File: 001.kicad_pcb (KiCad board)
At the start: 2 copper layers, 74.7 x 96.8 mm, 57 parts, among them J1 CONN_01X02, J10 TEST_1P, J11 TEST_1P, J12 TEST_1P, J13 TEST_1P, J14 TEST_1P, J15 TEST_1P, J16 TEST_1P, J2 TEST_1P, J3 TEST_1P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

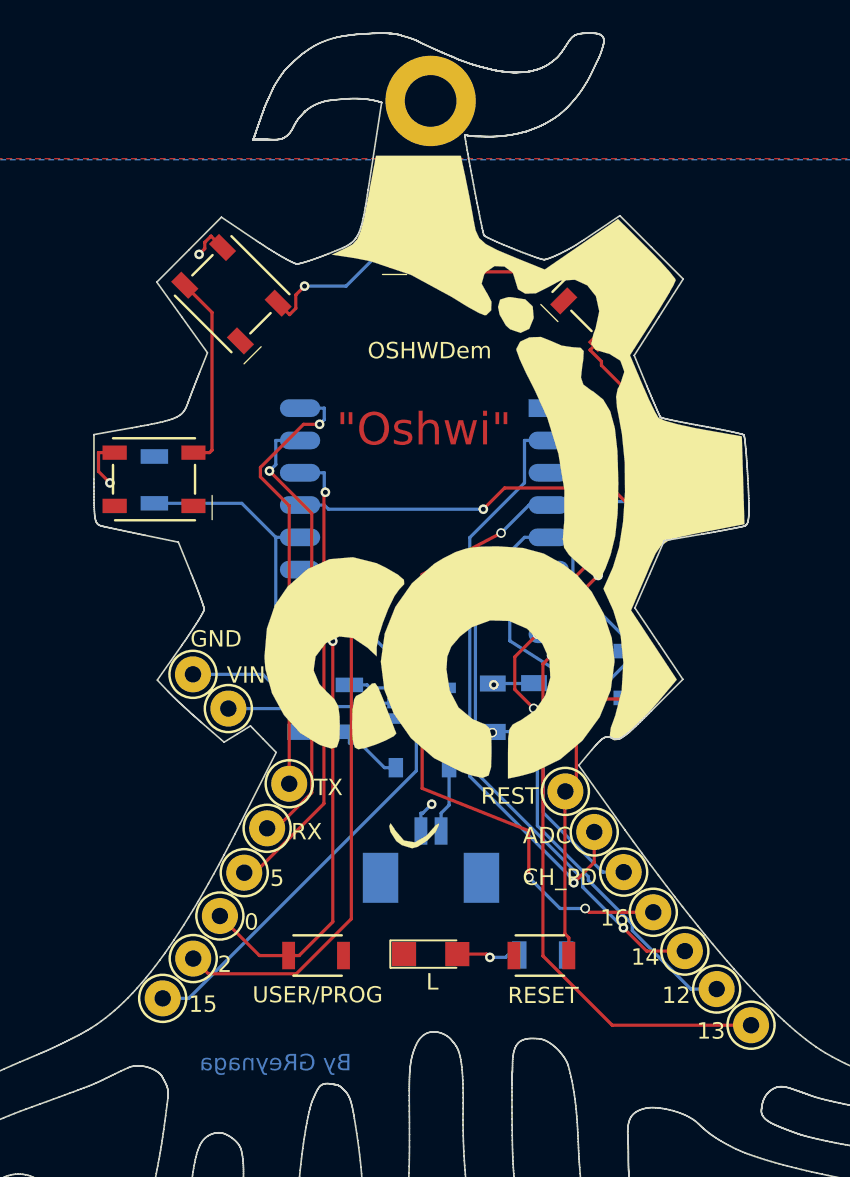
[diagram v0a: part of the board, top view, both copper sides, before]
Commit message: Final Release of OSHWDem Badge 2017
Final Release of OSHWDem Badge with PCBWay sponsorship
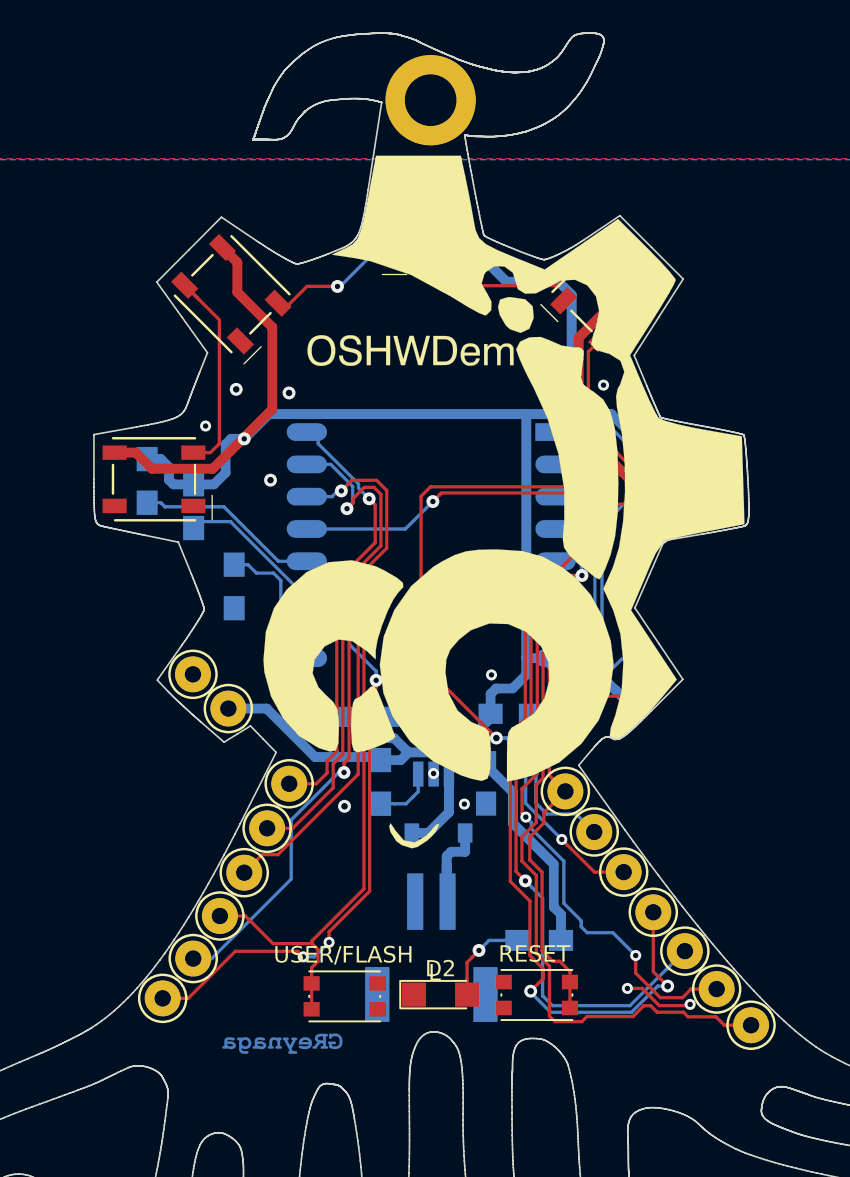
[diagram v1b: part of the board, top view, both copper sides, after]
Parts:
- removed G1***: LOGO, Mazmaker:mazmaker_700
- added BricoLabs-14***: LOGO, varios:bricolabs-14, B.Cu at (130.1, 52.3)
- added G***: LOGO, varios:OSHWDem-4, F.Cu at (129.4, 61.7)
- added GBSilk***: LOGO, varios:greynaga6-2, B.Cu at (121.3, 104.6)
- added GS***: v, varios:greynaga6-2-cooper, B.Cu at (121.3, 104.6)
- added PCBway-3: LOGO, varios:pcbway3, B.Cu at (145.1, 106.9)
- added R6: 10k, Resistors_SMD:R_0805_HandSoldering, B.Cu at (118.4, 76.4)
- added R7: 10k, Resistors_SMD:R_0805_HandSoldering, B.Cu at (115.8, 71.4)
- C1, C2, C3, C4: footprint Capacitors_SMD:C_1206 -> Capacitors_SMD:C_0805_HandSoldering
- J1: footprint Connectors_Molex:Molex_PicoBlade_53261-0271_02x1.25mm_Angled -> Connectors_JST:JST_PH_S2B-PH-SM4-TB_02x2.00mm_Angled
- R1, R2, R3, R4, R5: footprint Resistors_SMD:R_1206 -> Resistors_SMD:R_0805_HandSoldering
- SW1, SW2: footprint Wickerlib:SWITCH-OMRON-MOMENTARY-SMD-B3U-1000P -> kmr2:SW_SPST_KMR2
- moved J1 5.80 mm to (130.6, 98.8)
- moved R5 4.95 mm to (127.4, 88.5), turned to 270 degrees
- moved C2 4.71 mm to (133.9, 88.6), turned to 270 degrees
- moved C1 4.20 mm to (126.6, 84.5), turned to 180 degrees
- moved D1 4.17 mm to (131.0, 91.7)
- moved U2 3.13 mm to (130.7, 86.7), turned to 90 degrees
- moved R1 3.04 mm to (143.7, 71.4)
- moved SW2 2.83 mm to (137.1, 101.7)
- moved D2 2.58 mm to (131.1, 101.7)
- moved SW1 2.53 mm to (125.2, 101.8)
- moved U1 1.54 mm to (137.6, 66.8)
- moved C4 1.49 mm to (135.5, 84.3), turned to 0 degrees
- moved R2 0.93 mm to (137.2, 98.3)
- moved C3 0.56 mm to (146.8, 69.7)
- moved R4 0.51 mm to (143.2, 81.9)
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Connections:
- SW1 pad 2: GPIO0 -> GND
- SW2 pad 2: REST -> GND
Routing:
- net +3.3V: track 48.7 -> 161.1 mm, vias 13 -> 3
- net GND: track 24.0 -> 9.82 mm, vias 5 -> 20
- net REST: track 38.6 -> 48.1 mm
- net VCC: track 16.4 -> 25.3 mm
- net GPIO16: track 40.3 -> 48.6 mm
- net GPIO14: track 34.4 -> 42.6 mm, vias 1 -> 2
- net GPIO15: track 35.7 -> 43.6 mm, vias 0 -> 3
- net GPIO5: track 28.1 -> 34.9 mm
- net ADC: track 35.9 -> 42.4 mm, vias 1 -> 2
- net CH_PD: track 33.3 -> 37.9 mm, vias 0 -> 5
- net Net-(LED1-Pad4): track 12.1 -> 16.7 mm
- net GPIO13: track 39.8 -> 44.0 mm
- net GPIO12: track 35.4 -> 39.1 mm, vias 0 -> 3
- net GPIO0: track 45.7 -> 49.4 mm
- net RXD: track 28.9 -> 32.2 mm
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- added copper zone on B.Cu, net GND
- removed copper zone on B.Cu, net +3.3V
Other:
- net class Default: clearance 0.15 -> 0.1524; trace_width 0.2 -> 0.1524; via_dia 0.6 -> 0.6858; via_drill 0.4 -> 0.3302
- rule trace_clearance: 0.15 -> 0.1524
- rule trace_min: 0.1 -> 0.1524
- rule via_min_drill: 0.3 -> 0.3302
- rule via_min_size: 0.4 -> 0.6858
- board text added: "Designed by"
- board text added: "RESET"
- board text added: "USER/FLASH"
- board text removed: ""Oshwi""
- board text removed: "By GReynaga"
- board text removed: "Designed"
- board text removed: "MAZMAKER"
- board text removed: "OSHWDem"

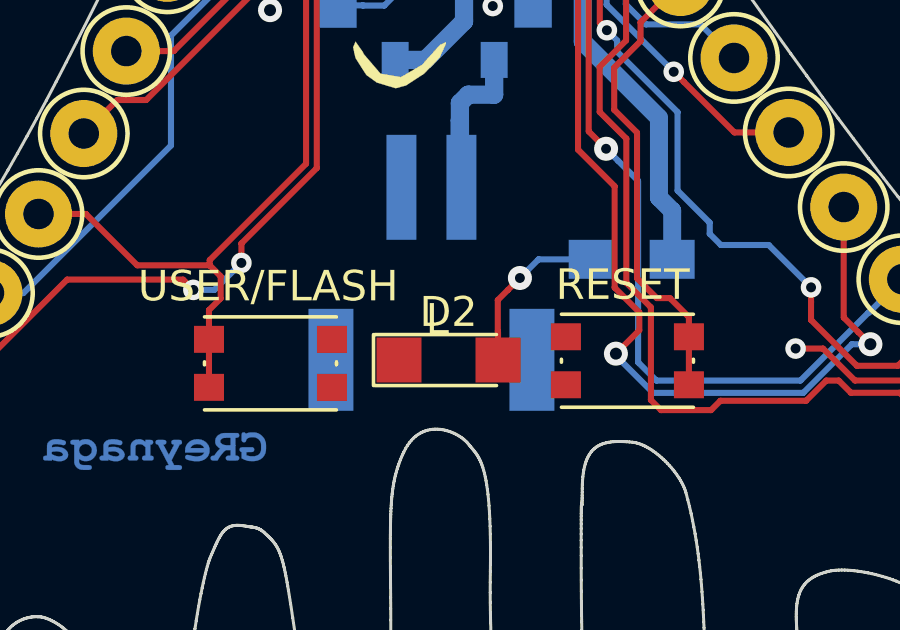
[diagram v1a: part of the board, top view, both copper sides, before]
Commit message: Change Label D2
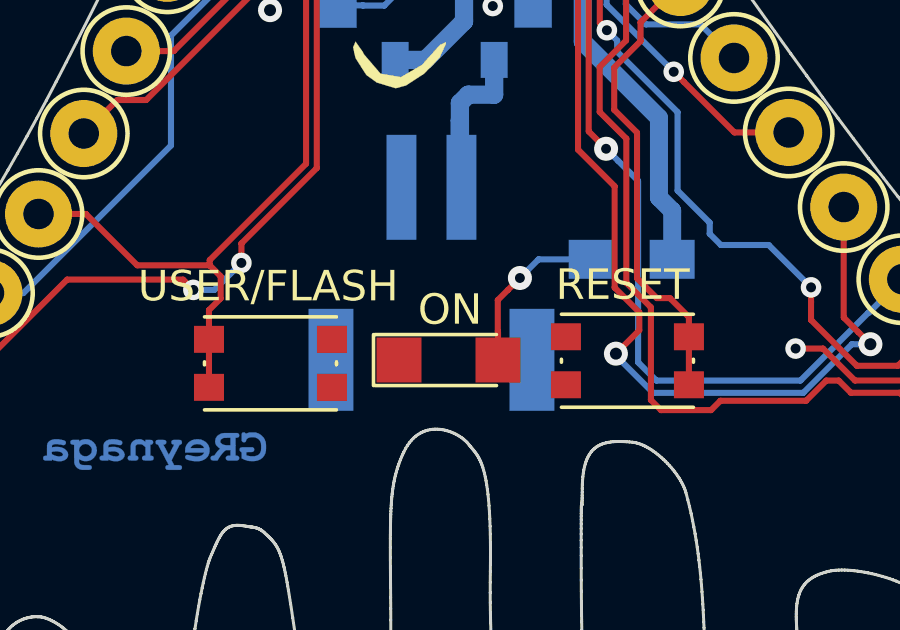
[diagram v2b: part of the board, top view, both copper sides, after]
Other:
- board text added: "ON"
- board text removed: "L"
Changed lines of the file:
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@@
   )
   (layers
-    (0 F.Cu signal)
-    (31 B.Cu signal)
+    (0 F.Cu signal hide)
+    (31 B.Cu signal hide)
     (33 F.Adhes user)
     (34 B.Paste user)
@@
     (tags "LED led 1206 SMD smd SMT smt smdled SMDLED smtled SMTLED")
     (attr smd)
-    (fp_text reference D2 (at 0 -1.6) (layer F.SilkS)
+    (fp_text reference D2 (at 0 -1.6) (layer F.SilkS) hide
       (effects (font (size 1 1) (thickness 0.15)))
     )
@@
     (effects (font (size 1.016 1.016) (thickness 0.1524)) (justify mirror))
   )
-  (gr_text L (at 130.75852 100.31752) (layer F.SilkS)
+  (gr_text ON (at 131.18 99.99) (layer F.SilkS)
     (effects (font (size 1.016 1.016) (thickness 0.1524)))
   )
